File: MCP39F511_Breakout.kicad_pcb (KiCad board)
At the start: 2 copper layers, 35.6 x 27.9 mm, 27 parts, among them J1 Conn_01x10, U1 MCP39F511-E_MQ, U2 MCP9700T-ETT, Y1 4MHz / 16pF

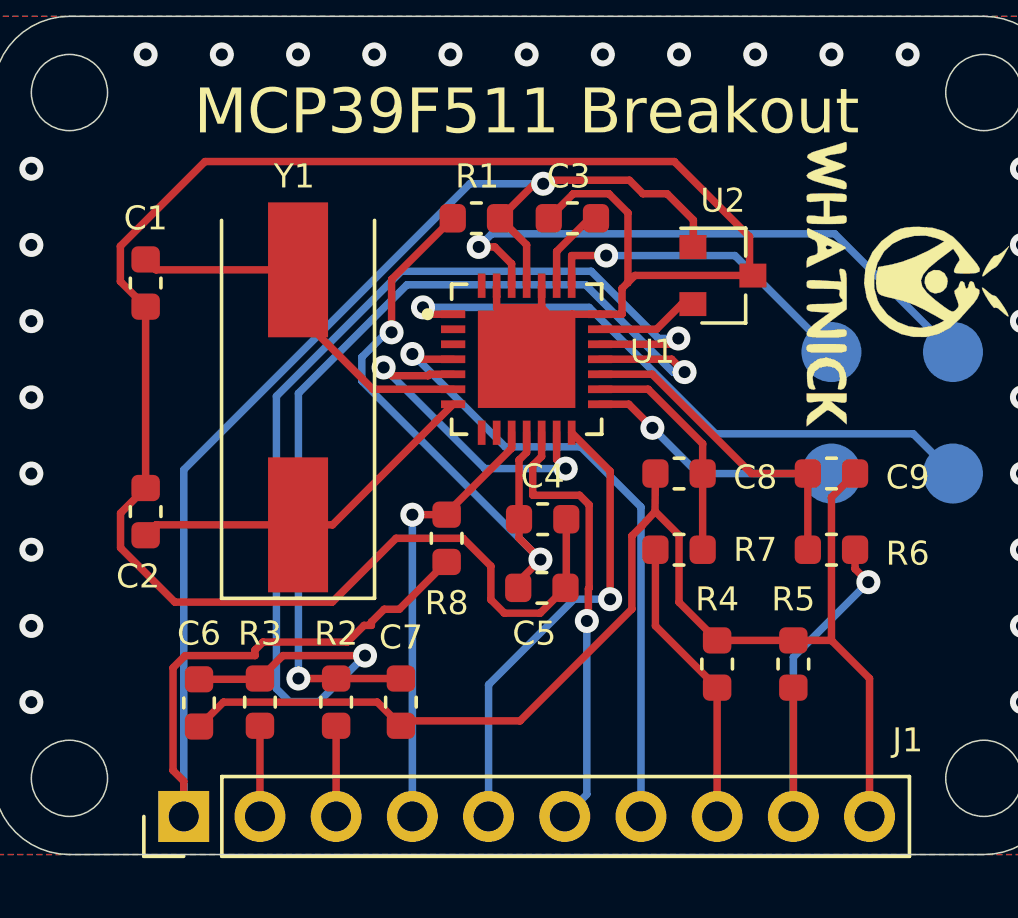
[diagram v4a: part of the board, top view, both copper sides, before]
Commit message: Add longer fillets to pads
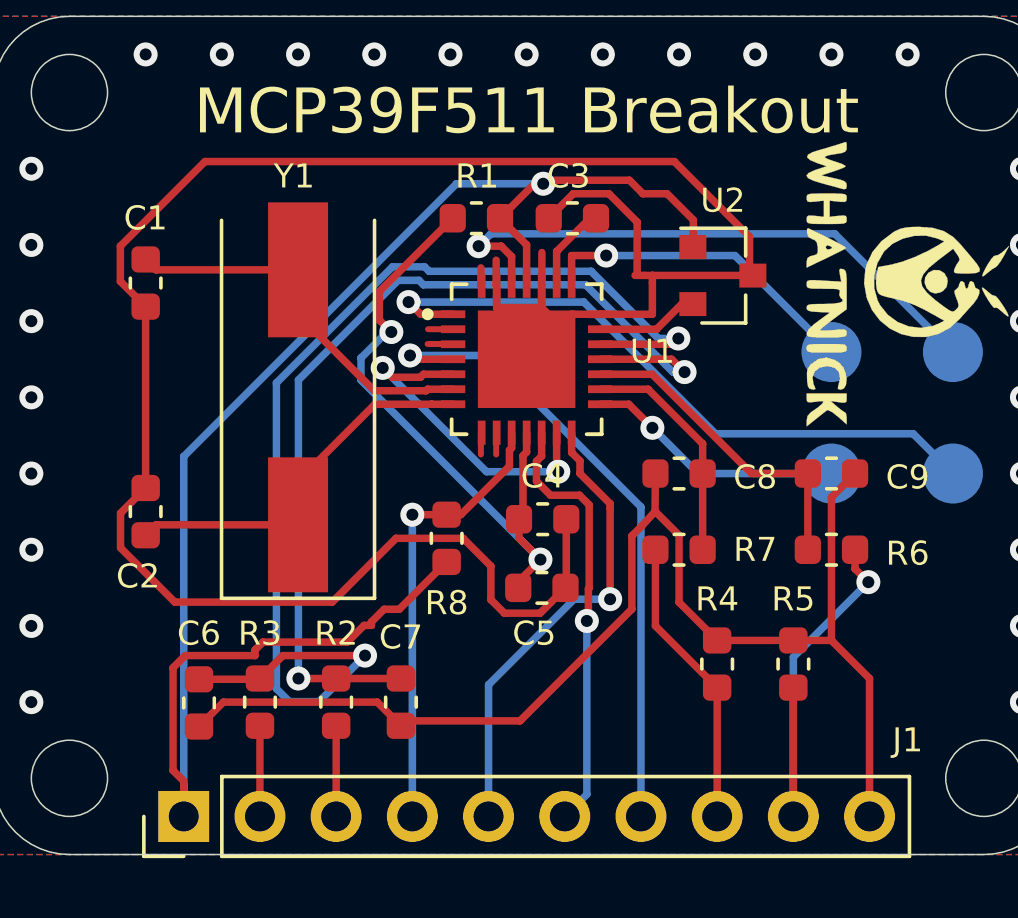
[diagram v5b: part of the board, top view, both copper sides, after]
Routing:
- net (no net): track 0.00 -> 3.16 mm
- net GND: track 118.0 -> 120.6 mm
- net Net-(TP2-Pad1): track 21.1 -> 22.2 mm
- net Net-(C2-Pad1): track 12.1 -> 12.9 mm
- net Net-(U1-Pad28): track 0.00 -> 0.60 mm

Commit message: New manufacture files
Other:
- board text added: "by Tisham Dhar http://whatnick.com v0.2 06/12/2020"
- board text removed: "by Tisham Dhar http://whatnick.com v0.1 16/11/2020"
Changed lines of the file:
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@@
     (effects (font (size 1 1) (thickness 0.2)) (justify mirror))
   )
-  (gr_text "by Tisham Dhar\nhttp://whatnick.com\nv0.1 16/11/2020" (at 128.905 94.615) (layer "B.SilkS")
+  (gr_text "by Tisham Dhar\nhttp://whatnick.com\nv0.2 06/12/2020" (at 128.905 94.615) (layer "B.SilkS")
     (effects (font (size 1 1) (thickness 0.25)) (justify mirror))
   )

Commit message: Add MCLR pullup
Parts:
- added R9: 10K, Resistor_SMD:R_0603_1608Metric, F.Cu at (142.9, 107.1)
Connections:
- net IIN+ renamed IINP
- net IIN- renamed IINN
- net VIN+ renamed VINP
- net VIN- renamed VINN
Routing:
- net +3V3: track 54.7 -> 71.9 mm, vias 1 -> 3
- net Net-(TP1-Pad1): track 19.8 -> 25.7 mm, vias 1 -> 2
- net (no net): track 3.16 -> 2.42 mm

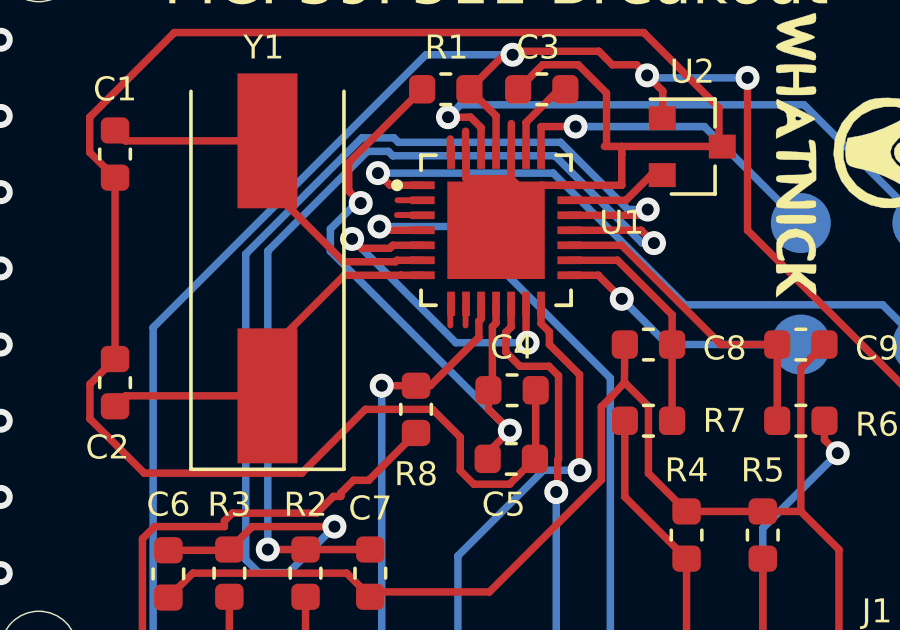
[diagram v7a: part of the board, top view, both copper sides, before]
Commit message: Schematic Cleanup, Notes added, PCB cleanup
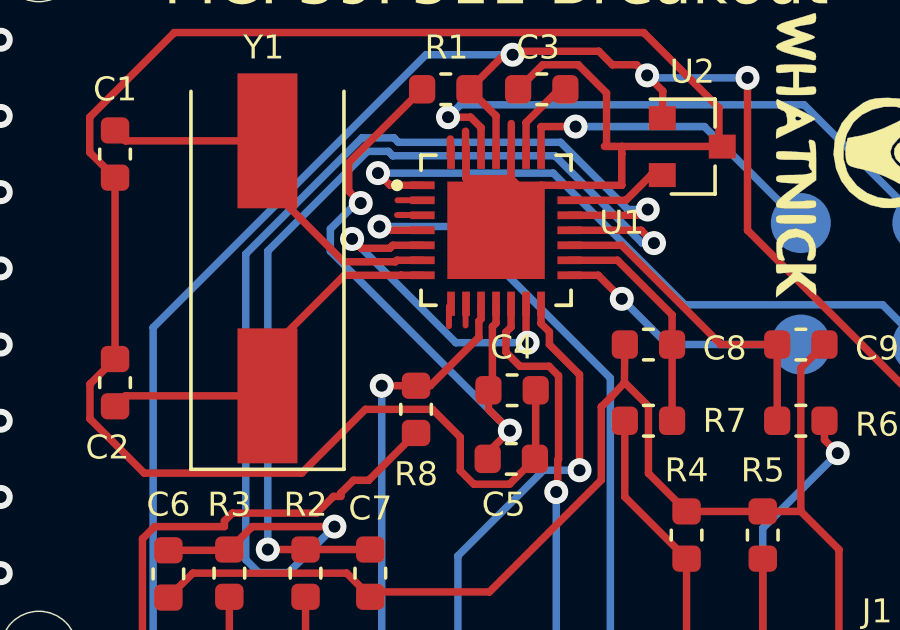
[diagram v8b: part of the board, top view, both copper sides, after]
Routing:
- net (no net): track 2.42 -> 3.20 mm
- net Net-(TP1-Pad1): track 25.7 -> 24.9 mm
